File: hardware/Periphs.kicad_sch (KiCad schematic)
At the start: 15 parts, among them J6 Conn_01x04, U1 TCAN4551RGYRQ1, Y2 7M40000005

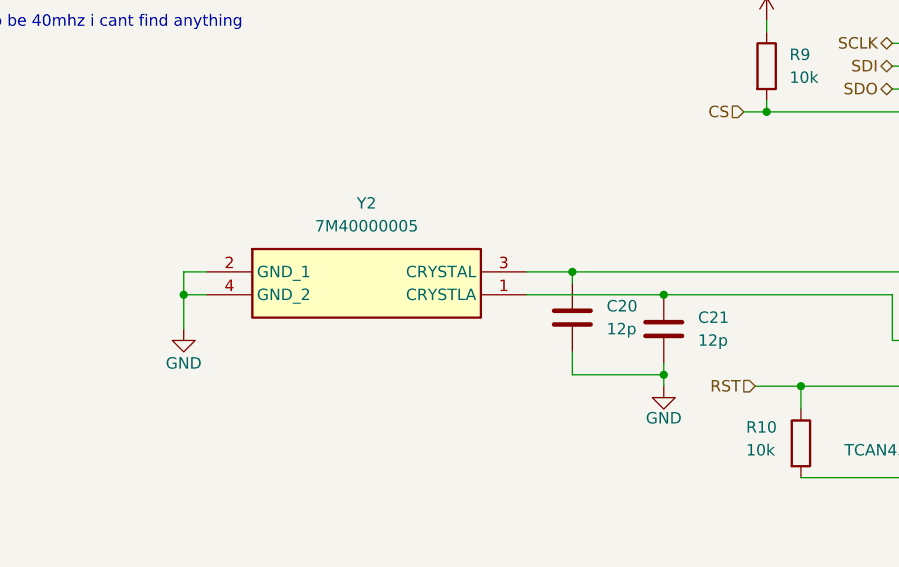
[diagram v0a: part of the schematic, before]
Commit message: changed pinout to match trs-star. also added resistors for spi
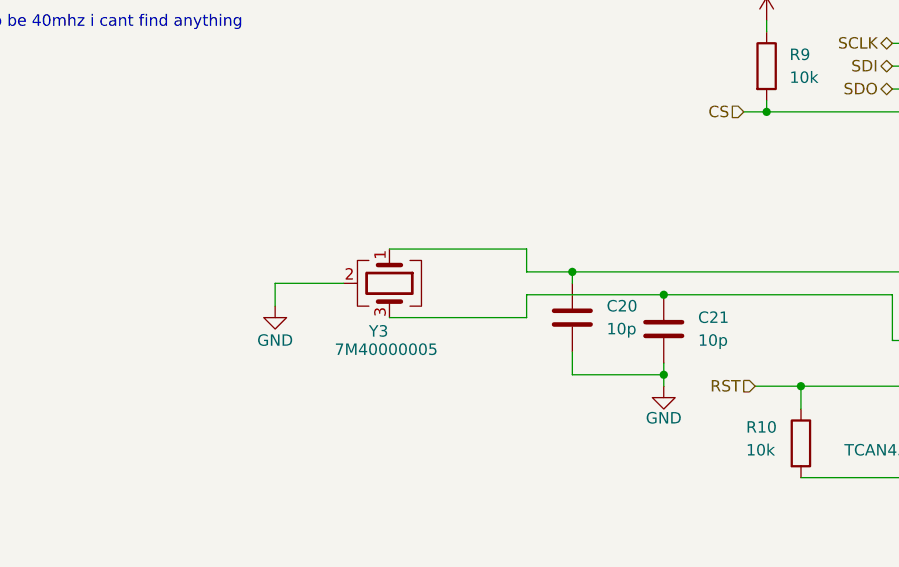
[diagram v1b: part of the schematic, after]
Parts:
- removed Y2: 7M40000005, 7M40000005:7M27120MAAJT, symbol 7M40000005:7M40000005
- added Y3: 7M40000005, 7M40000005:7M27120MAAJT, symbol Device:Crystal_GND24
- C20, C21: value 12p -> 10p
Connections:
- net GND: now also Y3.2 (G), Y3.4 (G)
- net at C21.1, U1.20 (OSC2): now also Y3.3
- net at C20.1, U1.1 (OSC1): now also Y3.1
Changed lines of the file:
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@@
 	)
 	(junction
-		(at 64.77 99.06)
-		(diameter 0)
-		(color 0 0 0 0)
-	)
-	(junction
 		(at 255.27 76.2)
 		(diameter 0)
@@
 	(wire
 		(pts
-			(xy 175.26 109.22) (xy 175.26 110.49)
+			(xy 102.87 101.6) (xy 102.87 99.06)
 		)
 		(stroke
@@
 	(wire
 		(pts
-			(xy 143.51 71.12) (xy 146.05 71.12)
+			(xy 175.26 109.22) (xy 175.26 110.49)
 		)
 		(stroke
@@
 	(wire
 		(pts
-			(xy 64.77 96.52) (xy 64.77 99.06)
+			(xy 143.51 71.12) (xy 146.05 71.12)
 		)
 		(stroke
@@
 	(wire
 		(pts
-			(xy 135.89 48.26) (xy 135.89 46.99)
+			(xy 87.63 93.98) (xy 102.87 93.98)
 		)
 		(stroke
@@
 	(wire
 		(pts
-			(xy 166.37 109.22) (xy 175.26 109.22)
+			(xy 135.89 48.26) (xy 135.89 46.99)
 		)
 		(stroke
@@
 	(wire
 		(pts
-			(xy 125.73 57.15) (xy 135.89 57.15)
+			(xy 166.37 109.22) (xy 175.26 109.22)
 		)
 		(stroke
@@
 	(wire
 		(pts
-			(xy 95.25 44.45) (xy 95.25 46.99)
+			(xy 125.73 57.15) (xy 135.89 57.15)
 		)
 		(stroke
@@
 	(wire
 		(pts
-			(xy 67.31 96.52) (xy 64.77 96.52)
+			(xy 95.25 44.45) (xy 95.25 46.99)
 		)
 		(stroke
@@
 	(wire
 		(pts
+			(xy 74.93 97.79) (xy 82.55 97.79)
+		)
+		(stroke
+			(width 0)
+			(type default)
+		)
+	)
+	(wire
+		(pts
 			(xy 156.21 119.38) (xy 156.21 121.92)
 		)
@@
 	(wire
 		(pts
-			(xy 64.77 99.06) (xy 67.31 99.06)
-		)
-		(stroke
-			(width 0)
-			(type default)
-		)
-	)
-	(wire
-		(pts
 			(xy 156.21 114.3) (xy 156.21 119.38)
 		)
@@
 	(wire
 		(pts
-			(xy 64.77 99.06) (xy 64.77 102.87)
-		)
-		(stroke
-			(width 0)
-			(type default)
-		)
-	)
-	(wire
-		(pts
 			(xy 118.11 99.06) (xy 143.51 99.06)
 		)
@@
 	(wire
 		(pts
+			(xy 87.63 101.6) (xy 102.87 101.6)
+		)
+		(stroke
+			(width 0)
+			(type default)
+		)
+	)
+	(wire
+		(pts
 			(xy 231.14 78.74) (xy 231.14 85.09)
 		)
@@
 	(wire
 		(pts
+			(xy 102.87 93.98) (xy 102.87 96.52)
+		)
+		(stroke
+			(width 0)
+			(type default)
+		)
+	)
+	(wire
+		(pts
 			(xy 107.95 105.41) (xy 107.95 107.95)
 		)
@@
 	(wire
 		(pts
+			(xy 74.93 100.33) (xy 74.93 97.79)
+		)
+		(stroke
+			(width 0)
+			(type default)
+		)
+	)
+	(wire
+		(pts
 			(xy 255.27 76.2) (xy 259.08 76.2)
 		)
@@
 	)
 	(symbol
+		(lib_id "Device:Crystal_GND24")
+		(at 87.63 97.79 270)
+		(unit 1)
+		(body_style 1)
+		(exclude_from_sim no)
+		(in_bom yes)
+		(on_board yes)
+		(in_pos_files yes)
+		(dnp no)
+		(property "Reference" "Y3"
+			(at 85.344 103.124 90)
+			(show_name no)
+			(do_not_autoplace no)
+			(effects
+				(font
+					(size 1.27 1.27)
+				)
+				(justify left)
+			)
+		)
+		(property "Value" "7M40000005"
+			(at 81.534 105.156 90)
+			(show_name no)
+			(do_not_autoplace no)
+			(effects
+				(font
+					(size 1.27 1.27)
+				)
+				(justify left)
+			)
+		)
+		(property "Footprint" "7M40000005:7M27120MAAJT"
+			(at 87.63 97.79 0)
+			(hide yes)
+			(show_name no)
+			(do_not_autoplace no)
+			(effects
+				(font
+					(size 1.27 1.27)
+				)
+			)
+		)
+		(property "Datasheet" "https://www.mouser.com/datasheet/3/827/1/7m.pdf"
+			(at 87.63 97.79 0)
+			(hide yes)
+			(show_name no)
+			(do_not_autoplace no)
+			(effects
+				(font
+					(size 1.27 1.27)
+				)
+			)
+		)
+		(property "Description" "Four pin crystal, GND on pins 2 and 4"
+			(at 87.63 97.79 0)
+			(hide yes)
+			(show_name no)
+			(do_not_autoplace no)
+			(effects
+				(font
+					(size 1.27 1.27)
+				)
+			)
+		)
+		(property private "KLC_S3.3" "The rectangle is not a symbol body but a graphical element"
+			(at 74.93 97.79 0)
+			(hide yes)
+			(show_name yes)
+			(do_not_autoplace no)
+			(effects
+				(font
+					(size 1.27 1.27)
+				)
+			)
+		)
+		(property private "KLC_S4.1" "Some pins are on 50mil grid to make the symbol small"
+			(at 72.39 97.79 0)
+			(hide yes)
+			(show_name yes)
+			(do_not_autoplace no)
+			(effects
+				(font
+					(size 1.27 1.27)
+				)
+			)
+		)
+		(pin "1"
+		)
+		(pin "4"
+		)
+		(pin "3"
+		)
+		(pin "2"
+		)
+		(instances
+			(project "OTTER"
+				(path "/db2a353b-4a3a-4ce7-8df7-bc33bc3b7cc7/eb093129-c761-474d-99d3-e85b871e9c74"
+					(reference "Y3")
+					(unit 1)
+				)
+			)
+		)
+	)
+	(symbol
 		(lib_id "power:GND")
 		(at 156.21 121.92 0)
@@
 			)
 		)
-		(property "Value" "12p"
+		(property "Value" "10p"
 			(at 121.92 104.1399 0)
 			(show_name no)
@@
 			)
 		)
-		(property "Value" "12p"
+		(property "Value" "10p"
 			(at 111.76 102.8699 0)
 			(show_name no)
@@
 	)
 	(symbol
-		(lib_id "7M40000005:7M40000005")
-		(at 67.31 96.52 0)
-		(unit 1)
-		(body_style 1)
-		(exclude_from_sim no)
-		(in_bom yes)
-		(on_board yes)
-		(in_pos_files yes)
-		(dnp no)
-		(fields_autoplaced yes)
-		(property "Reference" "Y2"
-			(at 85.09 88.9 0)
-			(show_name no)
-			(do_not_autoplace no)
-			(effects
-				(font
-					(size 1.27 1.27)
-				)
-			)
-		)
-		(property "Value" "7M40000005"
-			(at 85.09 91.44 0)
-			(show_name no)
-			(do_not_autoplace no)
-			(effects
-				(font
-					(size 1.27 1.27)
-				)
-			)
-		)
-		(property "Footprint" "7M40000005:7M27120MAAJT"
-			(at 99.06 191.44 0)
-			(hide yes)
-			(show_name no)
-			(do_not_autoplace no)
-			(effects
-				(font
-					(size 1.27 1.27)
-				)
-				(justify left top)
-			)
-		)
-		(property "Datasheet" "https://www.mouser.com/datasheet/3/827/1/7m.pdf"
-			(at 99.06 291.44 0)
-			(hide yes)
-			(show_name no)
-			(do_not_autoplace no)
-			(effects
-				(font
-					(size 1.27 1.27)
-				)
-				(justify left top)
-			)
-		)
-		(property "Description" "SMD Seam Sealing Crystals 3.2 x 2.5 x 0.7 mm 7M Series"
-			(at 74.168 104.648 0)
-			(hide yes)
-			(show_name no)
-			(do_not_autoplace no)
-			(effects
-				(font
-					(size 1.27 1.27)
-				)
-			)
-		)
-		(property "Height" "0.8"
-			(at 99.06 491.44 0)
-			(hide yes)
-			(show_name no)
-			(do_not_autoplace no)
-			(effects
-				(font
-					(size 1.27 1.27)
-				)
-				(justify left top)
-			)
-		)
-		(property "Mouser Part Number" "717-7M40000005"
-			(at 99.06 591.44 0)
-			(hide yes)
-			(show_name no)
-			(do_not_autoplace no)
-			(effects
-				(font
-					(size 1.27 1.27)
-				)
-				(justify left top)
-			)
-		)
-		(property "Mouser Price/Stock" "https://www.mouser.co.uk/ProductDetail/TXC-Corporation/7M40000005?qs=zQwgD8UkpXxLG%2FStvrkdqw%3D%3D"
-			(at 99.06 691.44 0)
-			(hide yes)
-			(show_name no)
-			(do_not_autoplace no)
-			(effects
-				(font
-					(size 1.27 1.27)
-				)
-				(justify left top)
-			)
-		)
-		(property "Manufacturer_Name" "TXC CORPORATION"
-			(at 99.06 791.44 0)
-			(hide yes)
-			(show_name no)
-			(do_not_autoplace no)
-			(effects
-				(font
-					(size 1.27 1.27)
-				)
-				(justify left top)
-			)
-		)
-		(property "Manufacturer_Part_Number" "7M40000005"
-			(at 99.06 891.44 0)
-			(hide yes)
-			(show_name no)
-			(do_not_autoplace no)
-			(effects
-				(font
-					(size 1.27 1.27)
-				)
-				(justify left top)
-			)
-		)
-		(pin "1"
-		)
-		(pin "2"
-		)
-		(pin "4"
-		)
-		(pin "3"
-		)
-		(instances
-			(project "OTTER"
-				(path "/db2a353b-4a3a-4ce7-8df7-bc33bc3b7cc7/eb093129-c761-474d-99d3-e85b871e9c74"
-					(reference "Y2")
-					(unit 1)
-				)
-			)
-		)
-	)
-	(symbol
 		(lib_id "power:GND")
 		(at 106.68 158.75 0)
@@
 	(symbol
 		(lib_id "power:GND")
-		(at 64.77 102.87 0)
+		(at 74.93 100.33 0)
 		(unit 1)
 		(body_style 1)
@@
 		(dnp no)
 		(property "Reference" "#PWR039"
-			(at 64.77 109.22 0)
+			(at 74.93 106.68 0)
 			(hide yes)
 			(show_name no)
@@
 		)
 		(property "Value" "GND"
-			(at 64.77 106.68 0)
+			(at 74.93 104.14 0)
 			(show_name no)
 			(do_not_autoplace no)
@@
 		)
 		(property "Footprint" ""
-			(at 64.77 102.87 0)
+			(at 74.93 100.33 0)
 			(hide yes)
 			(show_name no)
@@
 		)
 		(property "Datasheet" ""
-			(at 64.77 102.87 0)
+			(at 74.93 100.33 0)
 			(hide yes)
 			(show_name no)
@@
 		)
 		(property "Description" "Power symbol creates a global label with name \"GND\" , ground"
-			(at 64.77 102.87 0)
+			(at 74.93 100.33 0)
 			(hide yes)
 			(show_name no)

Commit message: some sort of placement done, need to fix up a lott...
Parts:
- added R18, R19, R20, R21: 22, Resistor_SMD:R_0603_1608Metric_Pad0.98x0.95mm_HandSolder, symbol Device:R
- added U2: USBLC6-4SC6, Package_TO_SOT_SMD:SOT-23-6, symbol Power_Protection:USBLC6-4SC6
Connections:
- net +12V is gone; now on net +20V: J6.4 (Pin_4)
- net +3.3V: now also U2.5 (VBUS)
- net CS: now also R21.1, U2.6 (I/O4); no longer U1.7 (~{CS})
- net GND: now also U2.2 (GND)
- net SCLK: now also R18.1, U2.1 (I/O1); no longer U1.4 (SCLK)
- net SDI: now also R19.1, U2.3 (I/O2); no longer U1.5 (SDI)
- net SDO: now also R20.1, U2.4 (I/O3); no longer U1.6 (SDO)
- new net: R18.2, U1.4 (SCLK)
- new net: R21.2, U1.7 (~{CS})
- new net: R20.2, U1.6 (SDO)
- new net: R19.2, U1.5 (SDI)
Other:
- note added: "ESD Protection"
- moved on the sheet: R9
